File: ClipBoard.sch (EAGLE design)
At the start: 11 parts, among them Q1 IRF520, Q2 IRF520, SW1 DPDT

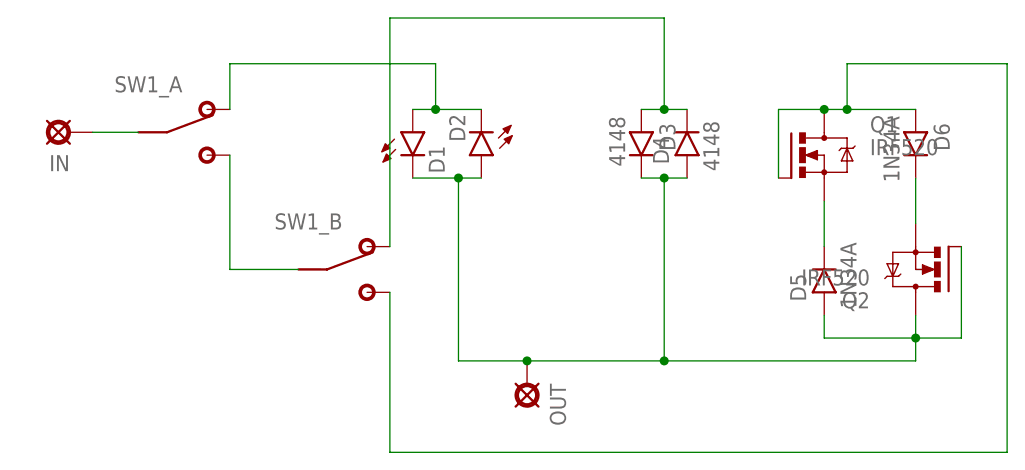
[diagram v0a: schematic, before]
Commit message: Changes to board and schematic to make v1.1
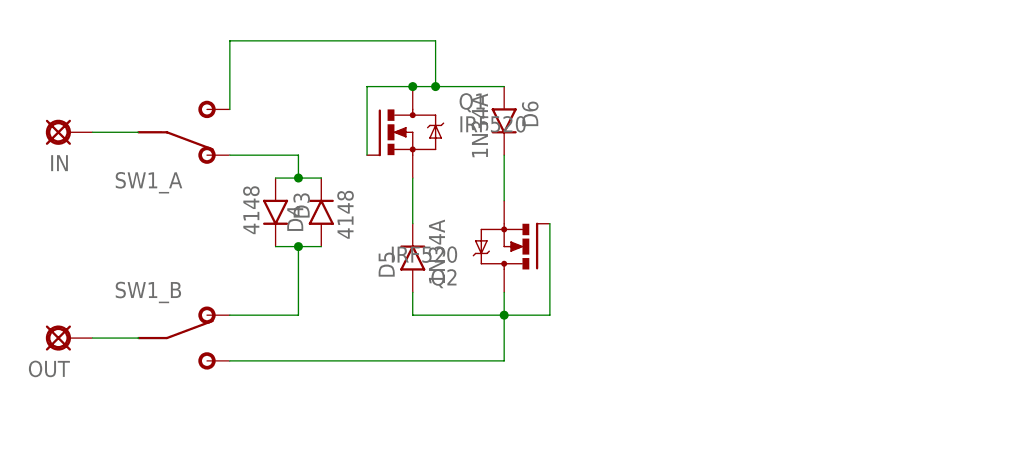
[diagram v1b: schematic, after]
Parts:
- removed D1, D2: 3MM, mb_diodes:LED3MM
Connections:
- removed net N$9: SW1_A.3, SW1_B.2
- new net N$3: OUT.PAD, SW1_B.2
- net N$1: now also D3.C, D4.A, SW1_B.1; no longer D1.A, D2.C, SW1_A.1
- net N$5: now also SW1_A.3; no longer SW1_B.3
- net N$7: now also SW1_A.1; no longer SW1_B.1
- net N$8: now also SW1_B.3; no longer D1.C, D2.A, D3.C, D4.A, OUT.PAD
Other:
- moved on the sheet: D3, D4, D5, D6, OUT, Q1, Q2, SW1_A, SW1_B
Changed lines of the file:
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@@
 <?xml version="1.0" encoding="utf-8"?>
 <!DOCTYPE eagle SYSTEM "eagle.dtd">
-<eagle version="7.2.0">
+<eagle version="7.1.0">
 <drawing>
 <settings>
@@
 <part name="IN" library="mb_supply" deviceset="PAD" device="" value="CLIPIN"/>
 <part name="OUT" library="mb_supply" deviceset="PAD" device="" value="CLIPOUT"/>
-<part name="D1" library="mb_diodes" deviceset="LED" device="3MM" value="3MM"/>
-<part name="D2" library="mb_diodes" deviceset="LED" device="3MM" value="3MM"/>
 <part name="D3" library="mb_diodes" deviceset="1N4148" device="-3" value="4148"/>
 <part name="D4" library="mb_diodes" deviceset="1N4148" device="-3" value="4148"/>
@@
 <instances>
 <instance part="IN" gate="G$1" x="-10.16" y="60.96" rot="R180"/>
-<instance part="OUT" gate="G$1" x="40.64" y="33.02" rot="R270"/>
-<instance part="D1" gate="G$1" x="27.94" y="58.42" rot="R90"/>
-<instance part="D2" gate="G$1" x="35.56" y="60.96" rot="R270"/>
-<instance part="D3" gate="G$1" x="53.34" y="58.42" rot="R270"/>
-<instance part="D4" gate="G$1" x="58.42" y="60.96" rot="R90"/>
-<instance part="Q1" gate="G$1" x="71.12" y="58.42"/>
-<instance part="Q2" gate="G$1" x="86.36" y="45.72" rot="R180"/>
-<instance part="D5" gate="G$1" x="73.66" y="45.72" rot="R90"/>
-<instance part="D6" gate="G$1" x="83.82" y="58.42" rot="R270"/>
-<instance part="SW1" gate="_A" x="2.54" y="60.96" rot="R270"/>
-<instance part="SW1" gate="_B" x="20.32" y="45.72" rot="R270"/>
+<instance part="OUT" gate="G$1" x="-10.16" y="38.1" rot="R180"/>
+<instance part="D3" gate="G$1" x="12.7" y="50.8" rot="R270"/>
+<instance part="D4" gate="G$1" x="17.78" y="53.34" rot="R90"/>
+<instance part="Q1" gate="G$1" x="25.4" y="60.96"/>
+<instance part="Q2" gate="G$1" x="40.64" y="48.26" rot="R180"/>
+<instance part="D5" gate="G$1" x="27.94" y="48.26" rot="R90"/>
+<instance part="D6" gate="G$1" x="38.1" y="60.96" rot="R270"/>
+<instance part="SW1" gate="_A" x="2.54" y="60.96" rot="MR90"/>
+<instance part="SW1" gate="_B" x="2.54" y="38.1" rot="R270"/>
 </instances>
 <busses>
 </busses>
 <nets>
-<net name="N$1" class="0">
-<segment>
-<pinref part="D1" gate="G$1" pin="A"/>
-<pinref part="D2" gate="G$1" pin="C"/>
-<wire x1="27.94" y1="63.5" x2="30.48" y2="63.5" width="0.1524" layer="91"/>
-<pinref part="SW1" gate="_A" pin="1"/>
-<wire x1="30.48" y1="63.5" x2="35.56" y2="63.5" width="0.1524" layer="91"/>
-<wire x1="7.62" y1="63.5" x2="7.62" y2="68.58" width="0.1524" layer="91"/>
-<wire x1="7.62" y1="68.58" x2="30.48" y2="68.58" width="0.1524" layer="91"/>
-<wire x1="30.48" y1="68.58" x2="30.48" y2="63.5" width="0.1524" layer="91"/>
-<junction x="30.48" y="63.5"/>
-</segment>
-</net>
 <net name="N$2" class="0">
 <segment>
 <pinref part="Q1" gate="G$1" pin="S"/>
 <pinref part="D5" gate="G$1" pin="C"/>
-<wire x1="73.66" y1="53.34" x2="73.66" y2="48.26" width="0.1524" layer="91"/>
+<wire x1="27.94" y1="55.88" x2="27.94" y2="50.8" width="0.1524" layer="91"/>
 </segment>
 </net>
@@
 <pinref part="Q2" gate="G$1" pin="S"/>
 <pinref part="D6" gate="G$1" pin="C"/>
-<wire x1="83.82" y1="50.8" x2="83.82" y2="55.88" width="0.1524" layer="91"/>
+<wire x1="38.1" y1="53.34" x2="38.1" y2="58.42" width="0.1524" layer="91"/>
 </segment>
 </net>
@@
 <pinref part="Q1" gate="G$1" pin="D"/>
 <pinref part="D6" gate="G$1" pin="A"/>
-<wire x1="83.82" y1="63.5" x2="76.2" y2="63.5" width="0.1524" layer="91"/>
+<wire x1="38.1" y1="66.04" x2="30.48" y2="66.04" width="0.1524" layer="91"/>
 <pinref part="Q1" gate="G$1" pin="G"/>
-<wire x1="76.2" y1="63.5" x2="73.66" y2="63.5" width="0.1524" layer="91"/>
-<wire x1="68.58" y1="55.88" x2="68.58" y2="63.5" width="0.1524" layer="91"/>
-<wire x1="68.58" y1="63.5" x2="73.66" y2="63.5" width="0.1524" layer="91"/>
-<junction x="73.66" y="63.5"/>
-<pinref part="SW1" gate="_B" pin="3"/>
-<wire x1="25.4" y1="43.18" x2="25.4" y2="25.4" width="0.1524" layer="91"/>
-<wire x1="25.4" y1="25.4" x2="93.98" y2="25.4" width="0.1524" layer="91"/>
-<wire x1="93.98" y1="25.4" x2="93.98" y2="68.58" width="0.1524" layer="91"/>
-<wire x1="93.98" y1="68.58" x2="76.2" y2="68.58" width="0.1524" layer="91"/>
-<wire x1="76.2" y1="68.58" x2="76.2" y2="63.5" width="0.1524" layer="91"/>
-<junction x="76.2" y="63.5"/>
+<wire x1="30.48" y1="66.04" x2="27.94" y2="66.04" width="0.1524" layer="91"/>
+<wire x1="22.86" y1="58.42" x2="22.86" y2="66.04" width="0.1524" layer="91"/>
+<wire x1="22.86" y1="66.04" x2="27.94" y2="66.04" width="0.1524" layer="91"/>
+<junction x="27.94" y="66.04"/>
+<wire x1="30.48" y1="71.12" x2="30.48" y2="66.04" width="0.1524" layer="91"/>
+<junction x="30.48" y="66.04"/>
+<pinref part="SW1" gate="_A" pin="3"/>
+<wire x1="7.62" y1="63.5" x2="7.62" y2="71.12" width="0.1524" layer="91"/>
+<wire x1="7.62" y1="71.12" x2="30.48" y2="71.12" width="0.1524" layer="91"/>
 </segment>
 </net>
@@
 <pinref part="D4" gate="G$1" pin="C"/>
 <pinref part="D3" gate="G$1" pin="A"/>
-<wire x1="53.34" y1="63.5" x2="55.88" y2="63.5" width="0.1524" layer="91"/>
-<pinref part="SW1" gate="_B" pin="1"/>
-<wire x1="55.88" y1="63.5" x2="58.42" y2="63.5" width="0.1524" layer="91"/>
-<wire x1="25.4" y1="48.26" x2="25.4" y2="73.66" width="0.1524" layer="91"/>
-<wire x1="25.4" y1="73.66" x2="55.88" y2="73.66" width="0.1524" layer="91"/>
-<wire x1="55.88" y1="73.66" x2="55.88" y2="63.5" width="0.1524" layer="91"/>
-<junction x="55.88" y="63.5"/>
+<wire x1="12.7" y1="55.88" x2="15.24" y2="55.88" width="0.1524" layer="91"/>
+<pinref part="SW1" gate="_A" pin="1"/>
+<wire x1="15.24" y1="55.88" x2="17.78" y2="55.88" width="0.1524" layer="91"/>
+<wire x1="7.62" y1="58.42" x2="15.24" y2="58.42" width="0.1524" layer="91"/>
+<wire x1="15.24" y1="58.42" x2="15.24" y2="55.88" width="0.1524" layer="91"/>
+<junction x="15.24" y="55.88"/>
 </segment>
 </net>
 <net name="N$8" class="0">
 <segment>
-<pinref part="D3" gate="G$1" pin="C"/>
-<pinref part="D4" gate="G$1" pin="A"/>
-<wire x1="53.34" y1="55.88" x2="55.88" y2="55.88" width="0.1524" layer="91"/>
-<pinref part="D1" gate="G$1" pin="C"/>
-<pinref part="D2" gate="G$1" pin="A"/>
-<wire x1="55.88" y1="55.88" x2="58.42" y2="55.88" width="0.1524" layer="91"/>
-<wire x1="27.94" y1="55.88" x2="33.02" y2="55.88" width="0.1524" layer="91"/>
-<pinref part="OUT" gate="G$1" pin="PAD"/>
-<wire x1="33.02" y1="55.88" x2="35.56" y2="55.88" width="0.1524" layer="91"/>
-<wire x1="33.02" y1="55.88" x2="33.02" y2="35.56" width="0.1524" layer="91"/>
-<wire x1="33.02" y1="35.56" x2="40.64" y2="35.56" width="0.1524" layer="91"/>
-<junction x="33.02" y="55.88"/>
-<wire x1="55.88" y1="55.88" x2="55.88" y2="35.56" width="0.1524" layer="91"/>
-<wire x1="55.88" y1="35.56" x2="40.64" y2="35.56" width="0.1524" layer="91"/>
-<junction x="55.88" y="55.88"/>
-<junction x="40.64" y="35.56"/>
 <pinref part="D5" gate="G$1" pin="A"/>
-<wire x1="73.66" y1="40.64" x2="73.66" y2="38.1" width="0.1524" layer="91"/>
-<wire x1="73.66" y1="38.1" x2="83.82" y2="38.1" width="0.1524" layer="91"/>
+<wire x1="27.94" y1="43.18" x2="27.94" y2="40.64" width="0.1524" layer="91"/>
+<wire x1="27.94" y1="40.64" x2="38.1" y2="40.64" width="0.1524" layer="91"/>
 <pinref part="Q2" gate="G$1" pin="D"/>
-<wire x1="83.82" y1="40.64" x2="83.82" y2="38.1" width="0.1524" layer="91"/>
+<wire x1="38.1" y1="43.18" x2="38.1" y2="40.64" width="0.1524" layer="91"/>
 <pinref part="Q2" gate="G$1" pin="G"/>
-<wire x1="88.9" y1="48.26" x2="88.9" y2="38.1" width="0.1524" layer="91"/>
-<wire x1="88.9" y1="38.1" x2="83.82" y2="38.1" width="0.1524" layer="91"/>
-<junction x="83.82" y="38.1"/>
-<wire x1="55.88" y1="35.56" x2="83.82" y2="35.56" width="0.1524" layer="91"/>
-<wire x1="83.82" y1="35.56" x2="83.82" y2="38.1" width="0.1524" layer="91"/>
-<junction x="55.88" y="35.56"/>
+<wire x1="43.18" y1="50.8" x2="43.18" y2="40.64" width="0.1524" layer="91"/>
+<wire x1="43.18" y1="40.64" x2="38.1" y2="40.64" width="0.1524" layer="91"/>
+<junction x="38.1" y="40.64"/>
+<pinref part="SW1" gate="_B" pin="3"/>
+<wire x1="7.62" y1="35.56" x2="38.1" y2="35.56" width="0.1524" layer="91"/>
+<wire x1="38.1" y1="35.56" x2="38.1" y2="40.64" width="0.1524" layer="91"/>
 </segment>
 </net>
-<net name="N$10" class="0">
+<net name="N$1" class="0">
+<segment>
+<pinref part="D4" gate="G$1" pin="A"/>
+<pinref part="D3" gate="G$1" pin="C"/>
+<wire x1="12.7" y1="48.26" x2="15.24" y2="48.26" width="0.1524" layer="91"/>
+<pinref part="SW1" gate="_B" pin="1"/>
+<wire x1="15.24" y1="48.26" x2="17.78" y2="48.26" width="0.1524" layer="91"/>
+<wire x1="7.62" y1="40.64" x2="15.24" y2="40.64" width="0.1524" layer="91"/>
+<wire x1="15.24" y1="40.64" x2="15.24" y2="48.26" width="0.1524" layer="91"/>
+<junction x="15.24" y="48.26"/>
+</segment>
+</net>
+<net name="N$6" class="0">
 <segment>
 <pinref part="IN" gate="G$1" pin="PAD"/>
@@
 </segment>
 </net>
-<net name="N$9" class="0">
+<net name="N$3" class="0">
 <segment>
-<pinref part="SW1" gate="_A" pin="3"/>
+<pinref part="OUT" gate="G$1" pin="PAD"/>
 <pinref part="SW1" gate="_B" pin="2"/>
-<wire x1="7.62" y1="58.42" x2="7.62" y2="45.72" width="0.1524" layer="91"/>
-<wire x1="7.62" y1="45.72" x2="15.24" y2="45.72" width="0.1524" layer="91"/>
+<wire x1="-7.62" y1="38.1" x2="-2.54" y2="38.1" width="0.1524" layer="91"/>
 </segment>
 </net>
